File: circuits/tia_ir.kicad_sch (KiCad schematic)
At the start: 11 parts, among them U1 OPA380AID

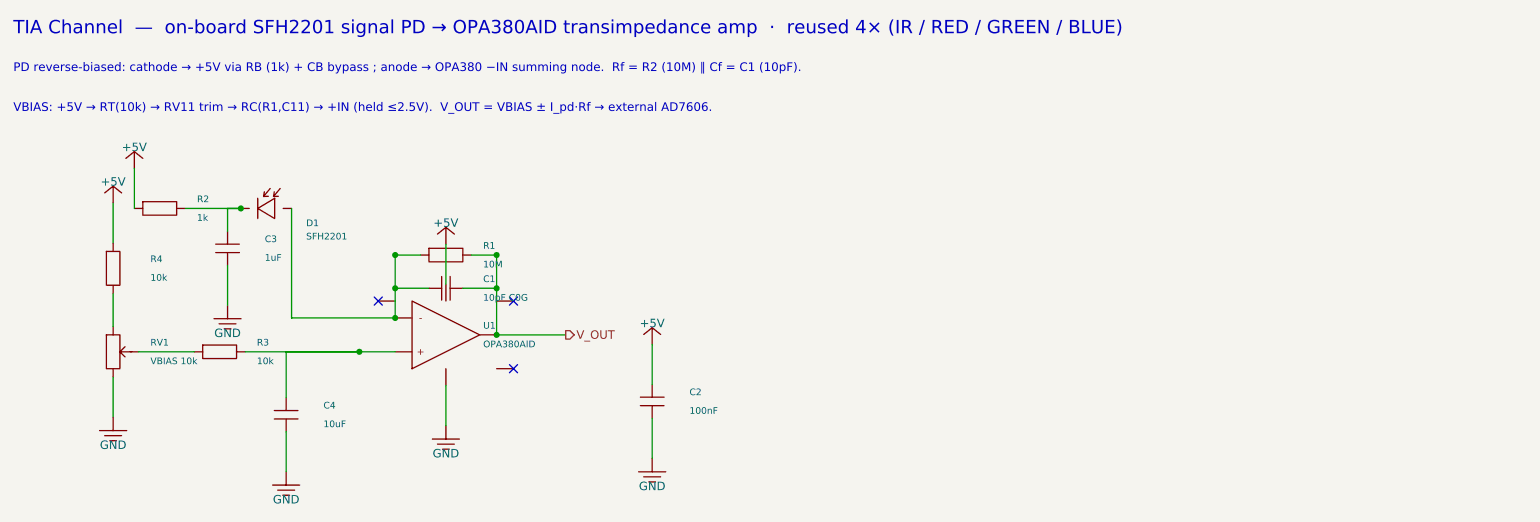
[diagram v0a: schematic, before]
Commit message: fix(circuits): import mcu sheet and laser footprints
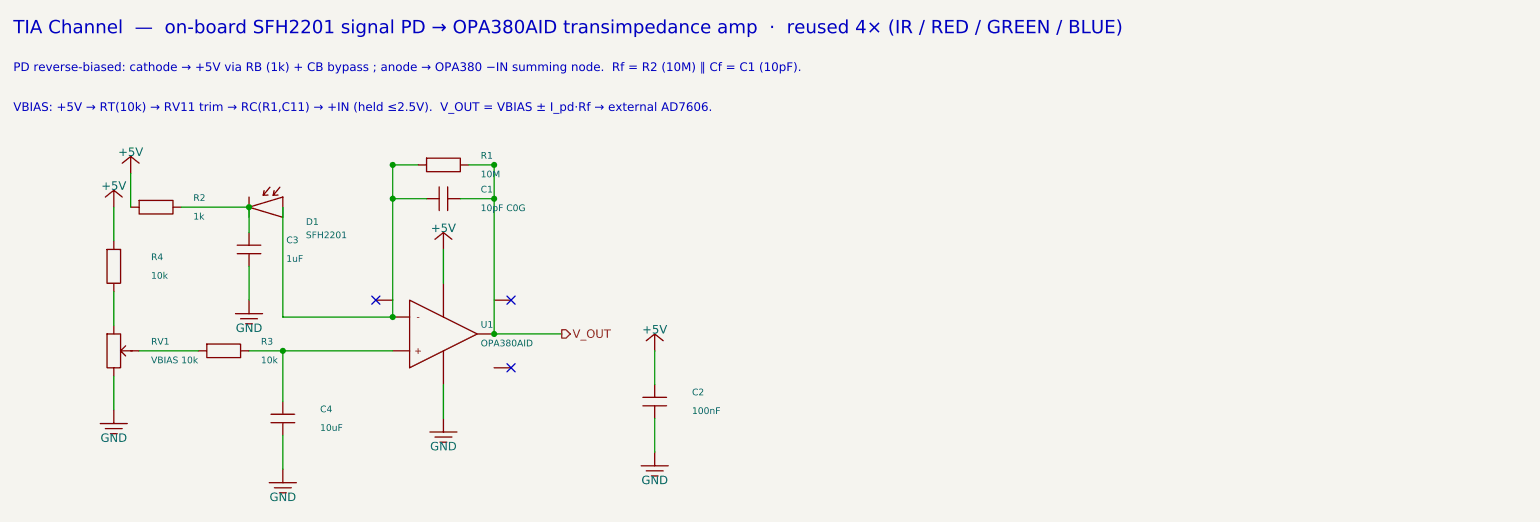
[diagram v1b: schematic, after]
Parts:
- C2: LCSC C1525 -> C83056; Part Number CL05B104KO5NNNC -> 0402B104K160CT
- C3: LCSC C52923 -> C7472946; Part Number CL05A105KA5NQNC -> HGC0402R5105K250NTEJ
- C4: LCSC C15850 -> C318691; Part Number CL21A106KAYNNNE -> CL21A106KAYNNNG
- R1: LCSC C57129 -> C844730; Part Number 0603WAF1005T5E -> CRCW060310M0FKEA
- R2: LCSC C21190 -> C2907002; Part Number 0603WAF1001T5E -> FRC0603F1001TS
- R3, R4: LCSC C269701 -> C844918; Part Number 0603WAF1002T5E -> CRCW060310K0FKEA
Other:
- moved on the sheet: C1, C3, C4, R1, R2, R3

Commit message: save laser controller schematic and layout state
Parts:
- RV5: renamed from R1; value 10M -> RF 2M; footprint Resistor_SMD:R_0603_1608Metric_Pad0.98x0.95mm_HandSolder -> Potentiometer_SMD:Potentiometer_Bourns_3224W_Vertical; symbol viv:R_H -> viv:POT_H; LCSC C844730 -> C116323; Part Number CRCW060310M0FKEA -> 3224W-1-205E
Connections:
- net V_OUT: now also RV5.3
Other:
- note added: "PD reverse-biased: cathode → +5V via RB (1k) + CB bypass ; anode → OPA380 −IN summing node. Rf = RVFB (2M trim) ∥ Cf = C1 (10pF)."
- note added: "VBIAS: +5V → RT(10k) → RV11 trim → RC(R1,C11) → +IN (held ≤2.5V). V_OUT = VBIAS ± I_pd·Rf → on-board AD7606-4."
- note removed: "PD reverse-biased: cathode → +5V via RB (1k) + CB bypass ; anode → OPA380 −IN summing node. Rf = R2 (10M) ∥ Cf = C1 (10pF)."
- note removed: "VBIAS: +5V → RT(10k) → RV11 trim → RC(R1,C11) → +IN (held ≤2.5V). V_OUT = VBIAS ± I_pd·Rf → external AD7606."
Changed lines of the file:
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@@
     )
   )
-  (symbol (lib_id "viv:R_H") (at 214.63 124.46 0) (unit 1)
-    (in_bom yes) (on_board yes) (dnp no)
-    (property "Reference" "R1" (at 220.23 123.06 0) (effects (font (size 1.0 1.0)) (justify left)))
-    (property "Value" "10M" (at 220.23 125.86 0) (effects (font (size 1.0 1.0)) (justify left)))
-    (property "Footprint" "Resistor_SMD:R_0603_1608Metric_Pad0.98x0.95mm_HandSolder" (at 214.63 124.46 0) (effects (font (size 1.0 1.0)) hide))
+  (symbol (lib_id "viv:POT_H") (at 214.63 124.46 0) (unit 1)
+    (in_bom yes) (on_board yes) (dnp no)
+    (property "Reference" "RV5" (at 220.23 123.06 0) (effects (font (size 1.0 1.0)) (justify left)))
+    (property "Value" "RF 2M" (at 220.23 125.86 0) (effects (font (size 1.0 1.0)) (justify left)))
+    (property "Footprint" "Potentiometer_SMD:Potentiometer_Bourns_3224W_Vertical" (at 214.63 124.46 0) (effects (font (size 1.0 1.0)) hide))
     (property "Datasheet" "" (at 214.63 124.46 0) (effects (font (size 1.0 1.0)) hide))
-    (property "Part Number" "CRCW060310M0FKEA" (at 214.63 124.46 0) (effects (font (size 1.0 1.0)) hide))
-    (property "LCSC" "C844730" (at 214.63 124.46 0) (effects (font (size 1.0 1.0)) hide))
-    (pin "1")
-    (pin "2")
-    (instances
-      (project "laser_controller"
-        (path "/c1d2e3f4-6000-4000-a000-000000000001" (reference "R1") (unit 1))
+    (property "Part Number" "3224W-1-205E" (at 214.63 124.46 0) (effects (font (size 1.0 1.0)) hide))
+    (property "LCSC" "C116323" (at 214.63 124.46 0) (effects (font (size 1.0 1.0)) hide))
+    (pin "1")
+    (pin "2")
+    (pin "3")
+    (instances
+      (project "laser_controller"
+        (path "/c1d2e3f4-6000-4000-a000-000000000001" (reference "RV5") (unit 1))
       )
     )
@@
   (wire (pts (xy 210.82 124.46) (xy 207.01 124.46)) (stroke (width 0) (type default)))
   (wire (pts (xy 218.44 124.46) (xy 222.25 124.46)) (stroke (width 0) (type default)))
+  (wire (pts (xy 214.63 120.65) (xy 222.25 120.65)) (stroke (width 0) (type default)))
+  (wire (pts (xy 222.25 120.65) (xy 222.25 124.46)) (stroke (width 0) (type default)))
   (wire (pts (xy 212.09 129.54) (xy 207.01 129.54)) (stroke (width 0) (type default)))
   (wire (pts (xy 217.17 129.54) (xy 222.25 129.54)) (stroke (width 0) (type default)))
@@
   (hierarchical_label "V_OUT" (shape output) (at 232.41 149.86 0) (effects (font (size 1.27 1.27)) (justify left)))
   (text "TIA Channel  —  on-board SFH2201 signal PD → OPA380AID transimpedance amp  ·  reused 4× (IR / RED / GREEN / BLUE)" (at 150 104 0) (effects (font (size 2.0 2.0)) (justify left)))
-  (text "PD reverse-biased: cathode → +5V via RB (1k) + CB bypass ; anode → OPA380 −IN summing node.  Rf = R2 (10M) ∥ Cf = C1 (10pF)." (at 150 110 0) (effects (font (size 1.3 1.3)) (justify left)))
-  (text "VBIAS: +5V → RT(10k) → RV11 trim → RC(R1,C11) → +IN (held ≤2.5V).  V_OUT = VBIAS ± I_pd·Rf → external AD7606." (at 150 116 0) (effects (font (size 1.3 1.3)) (justify left)))
+  (text "PD reverse-biased: cathode → +5V via RB (1k) + CB bypass ; anode → OPA380 −IN summing node.  Rf = RVFB (2M trim) ∥ Cf = C1 (10pF)." (at 150 110 0) (effects (font (size 1.3 1.3)) (justify left)))
+  (text "VBIAS: +5V → RT(10k) → RV11 trim → RC(R1,C11) → +IN (held ≤2.5V).  V_OUT = VBIAS ± I_pd·Rf → on-board AD7606-4." (at 150 116 0) (effects (font (size 1.3 1.3)) (justify left)))
   (sheet_instances
     (path "/" (page "1"))
